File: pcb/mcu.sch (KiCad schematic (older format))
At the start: 13 parts, among them J2 CONN_INTEGRALSTICK_MCU_DEVICE, U1 STM32F777NIH6‎, U10 DSC6083MI2A-032K768, U2 XC7A50T-1FTG256C, U6 S25FL064LABNFI011‎

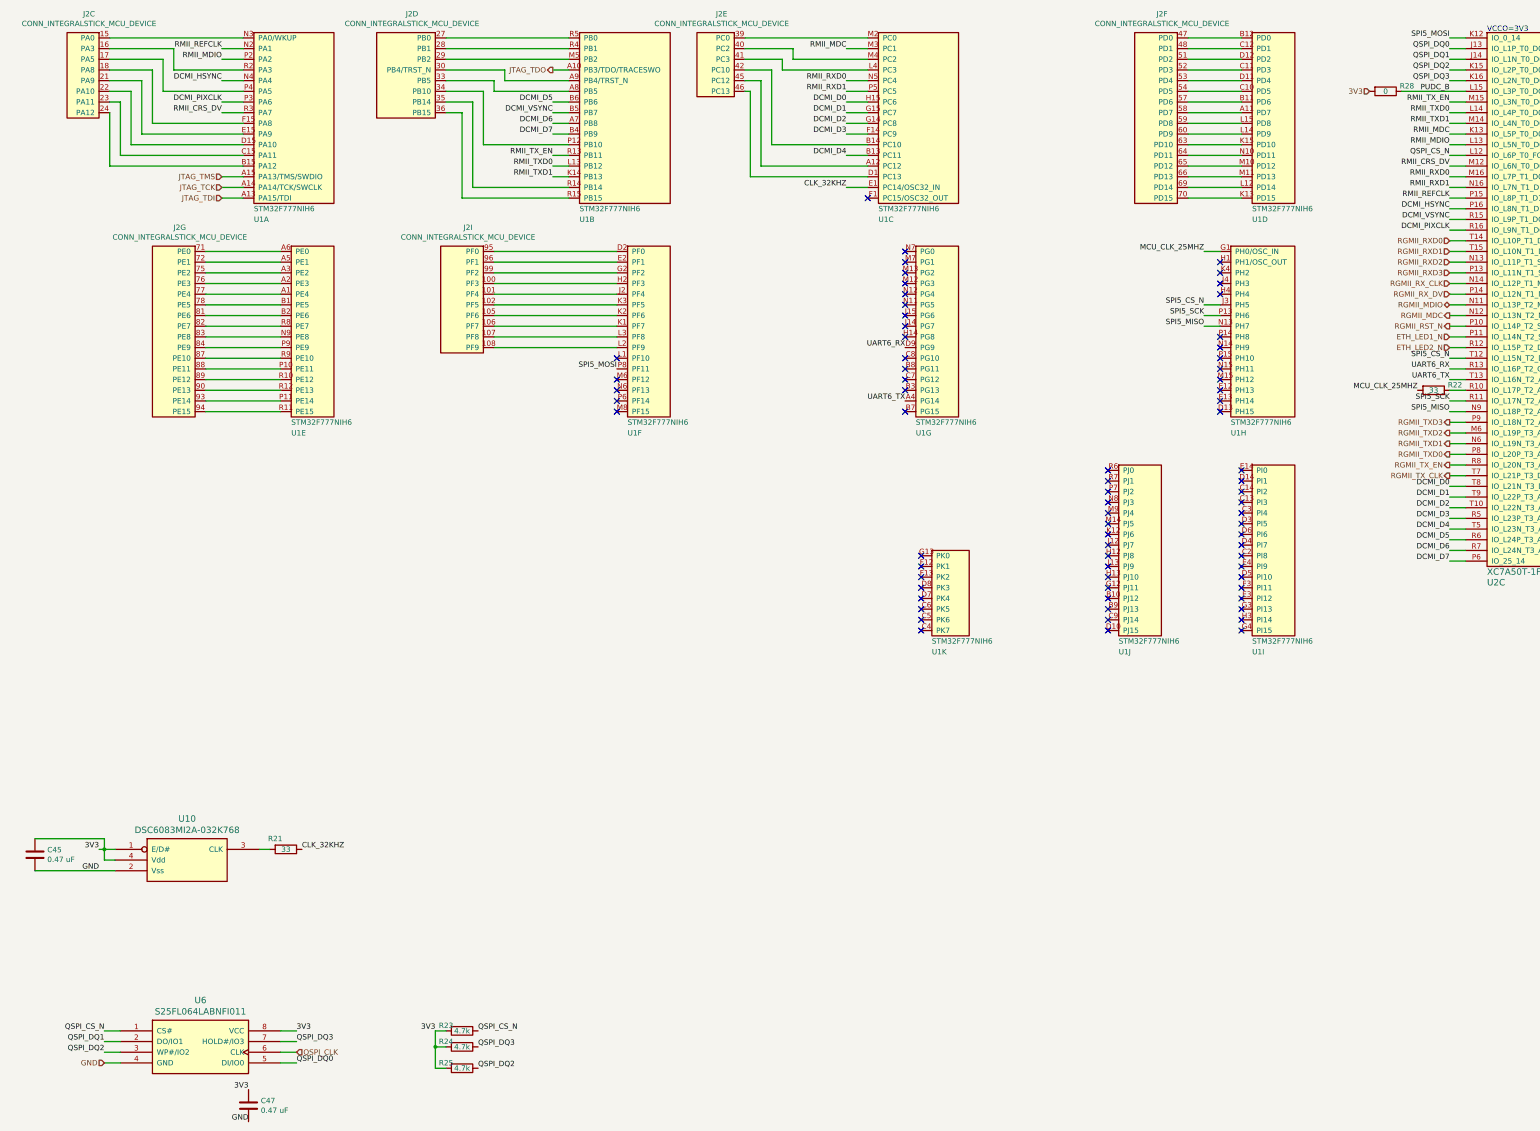
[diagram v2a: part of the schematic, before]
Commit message: Finished schematic signoff review. Fixed oscillator pinout bug, added some test points.
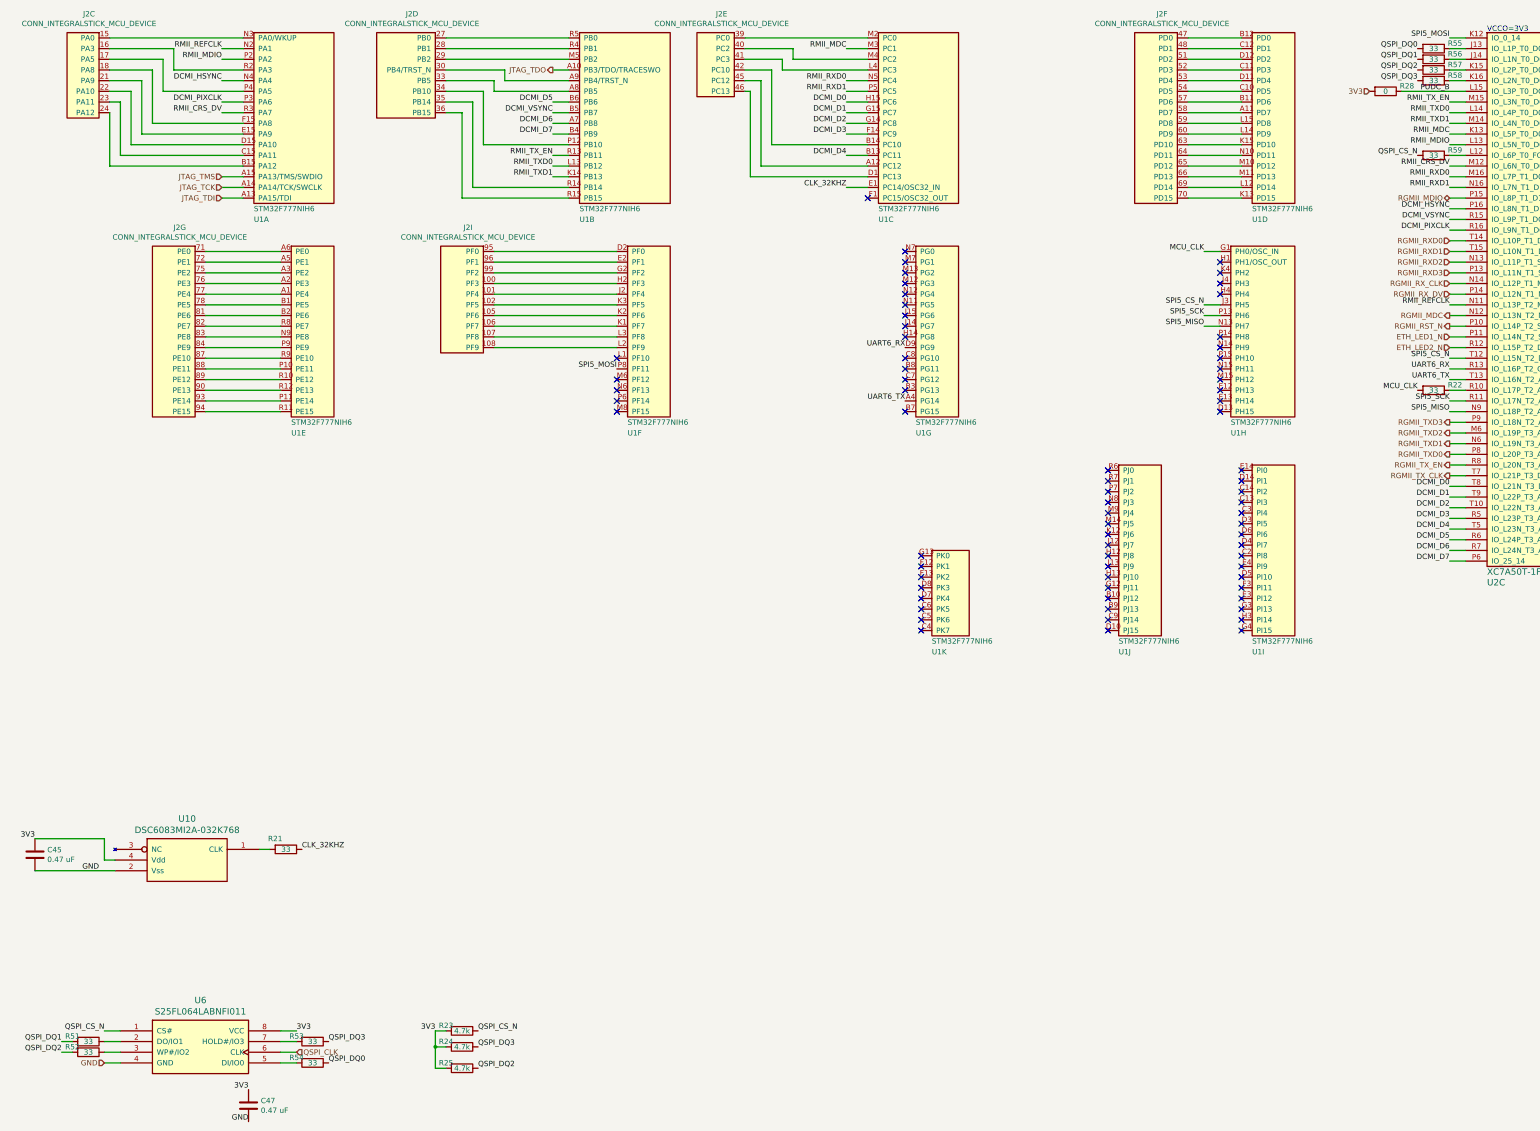
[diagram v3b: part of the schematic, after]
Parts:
- removed U10: DSC6083MI2A-032K768, symbol osc-azonenberg:OSC
- added R51, R52, R53, R54, R55, R56, R57, R58, R59: 33, symbol device:R
- added U10: DSC6083MI2A-032K768, symbol osc-azonenberg:DSC6083
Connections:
- net 3V3: now also U10.4 (Vdd)
- net GND: now also U10.2 (Vss)
- net QSPI_CS_N: now also R59.2; no longer U2.L12 (IO_L6P_T0_FCS_B_14)
- net QSPI_DQ0: now also R54.1, R55.2; no longer U2.J13 (IO_L1P_T0_D00_MOSI_14), U6.5 (DI/IO0)
- net QSPI_DQ1: now also R51.2, R56.2; no longer U2.J14 (IO_L1N_T0_D01_DIN_14), U6.2 (DO/IO1)
- net QSPI_DQ2: now also R52.2, R57.2; no longer U2.K15 (IO_L2P_T0_D02_14), U6.3 (WP#/IO2)
- net QSPI_DQ3: now also R53.1, R58.2; no longer U2.K16 (IO_L2N_T0_D03_14), U6.7 (HOLD#/IO3)
- net RGMII_MDIO: now also U2.P15 (IO_L8P_T1_D11_14); no longer U2.N11 (IO_L13P_T2_MRCC_14)
- net RMII_REFCLK: now also U2.N11 (IO_L13P_T2_MRCC_14); no longer U2.P15 (IO_L8P_T1_D11_14)
- net at R21.2: now also U10.1 (CLK)
- net MCU_CLK_25MHZ renamed MCU_CLK
- new net: R55.1, U2.J13 (IO_L1P_T0_D00_MOSI_14)
- new net: R56.1, U2.J14 (IO_L1N_T0_D01_DIN_14)
- new net: R57.1, U2.K15 (IO_L2P_T0_D02_14)
- new net: R58.1, U2.K16 (IO_L2N_T0_D03_14)
- new net: R59.1, U2.L12 (IO_L6P_T0_FCS_B_14)
- new net: R51.1, U6.2 (DO/IO1)
- new net: R52.1, U6.3 (WP#/IO2)
- new net: R54.2, U6.5 (DI/IO0)
- new net: R53.2, U6.7 (HOLD#/IO3)
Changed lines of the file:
@@
 Sheet 8 8
 Title "INTEGRALSTICK Compute Module"
-Date "2018-11-07"
+Date "2018-11-09"
 Rev "0.1"
 Comp "Andrew D. Zonenberg"
@@
 Text Label 13950 5450 2    50   ~ 0
 DCMI_D4
-Text Label 13950 2350 2    50   ~ 0
+Text Label 13950 3350 2    50   ~ 0
 RMII_REFCLK
 Text Label 13950 1850 2    50   ~ 0
@@
 Wire Wire Line
 	1350 10450 1500 10450
-Text Label 3150 10450 0    50   ~ 0
+Text Label 3450 10450 0    50   ~ 0
 QSPI_DQ0
-Text Label 1350 10250 2    50   ~ 0
+Text Label 950  10250 2    50   ~ 0
 QSPI_DQ1
 Text Label 1350 10150 2    50   ~ 0
@@
 Wire Wire Line
 	3150 10450 3000 10450
-Text Label 1350 10350 2    50   ~ 0
+Text Label 950  10350 2    50   ~ 0
 QSPI_DQ2
-Text Label 3150 10250 0    50   ~ 0
+Text Label 3450 10250 0    50   ~ 0
 QSPI_DQ3
 Wire Wire Line
@@
 Wire Wire Line
 	3000 10250 3150 10250
-Text Label 13950 950  2    50   ~ 0
+Text Label 13650 950  2    50   ~ 0
 QSPI_DQ0
-Text Label 13950 1050 2    50   ~ 0
+Text Label 13650 1050 2    50   ~ 0
 QSPI_DQ1
-Text Label 13950 1150 2    50   ~ 0
+Text Label 13650 1150 2    50   ~ 0
 QSPI_DQ2
-Text Label 13950 1250 2    50   ~ 0
+Text Label 13650 1250 2    50   ~ 0
 QSPI_DQ3
 Wire Wire Line
@@
 Wire Wire Line
 	14100 950  13950 950
-Text Label 13950 1950 2    50   ~ 0
+Text Label 13650 1950 2    50   ~ 0
 QSPI_CS_N
 Wire Wire Line
@@
 	13950 2250 14100 2250
 Wire Wire Line
-	14100 2350 13950 2350
+	14100 3350 13950 3350
 Wire Wire Line
 	14100 2650 13950 2650
@@
 Wire Wire Line
 	14100 3250 13950 3250
-Text HLabel 13950 3350 0    50   BiDi ~ 0
+Text HLabel 13950 2350 0    50   BiDi ~ 0
 RGMII_MDIO
 Text HLabel 13950 3450 0    50   Output ~ 0
@@
 	13950 3450 14100 3450
 Wire Wire Line
-	14100 3350 13950 3350
+	14100 2350 13950 2350
 Text HLabel 13950 3550 0    50   Output ~ 0
 RGMII_RST_N
@@
 GND
 NoConn ~ 11800 2950
-$Comp
-L osc-azonenberg:OSC U10
-U 1 1 5BE5F5BA
-P 2150 8450
-F 0 "U10" H 2125 8737 60  0000 C CNN
-F 1 "DSC6083MI2A-032K768" H 2125 8631 60  0000 C CNN
-F 2 "" H 2150 8450 60  0000 C CNN
-F 3 "" H 2150 8450 60  0000 C CNN
-	1    2150 8450
-	1    0    0    -1
-$EndComp
-Text Label 1300 8450 2    50   ~ 0
+Text Label 700  8350 2    50   ~ 0
 3V3
 Wire Wire Line
-	1300 8450 1350 8450
-Wire Wire Line
-	1350 8450 1350 8550
-Wire Wire Line
 	1350 8550 1450 8550
-Connection ~ 1350 8450
-Wire Wire Line
-	1350 8450 1450 8450
 Text Label 1300 8650 2    50   ~ 0
 GND
@@
 Wire Wire Line
 	700  8350 1350 8350
-Wire Wire Line
-	1350 8350 1350 8450
 Text Label 8300 2250 2    50   ~ 0
 CLK_32KHZ
@@
 $EndComp
 Text Label 13650 4150 2    50   ~ 0
-MCU_CLK_25MHZ
+MCU_CLK
 Text Label 11650 2850 2    50   ~ 0
-MCU_CLK_25MHZ
+MCU_CLK
 Wire Wire Line
 	11650 2850 11800 2850
@@
 Wire Wire Line
 	13950 4350 14100 4350
+$Comp
+L osc-azonenberg:DSC6083 U10
+U 1 1 5D305E88
+P 2150 8450
+F 0 "U10" H 2125 8737 60  0000 C CNN
+F 1 "DSC6083MI2A-032K768" H 2125 8631 60  0000 C CNN
+F 2 "" H 2150 8450 60  0000 C CNN
+F 3 "" H 2150 8450 60  0000 C CNN
+	1    2150 8450
+	1    0    0    -1
+$EndComp
+Wire Wire Line
+	1350 8350 1350 8550
+$Comp
+L device:R R53
+U 1 1 5D3680F9
+P 3300 10250
+F 0 "R53" V 3250 10100 50  0000 C CNN
+F 1 "33" V 3300 10250 50  0000 C CNN
+F 2 "" V 3230 10250 50  0001 C CNN
+F 3 "" H 3300 10250 50  0001 C CNN
+	1    3300 10250
+	0    1    1    0
+$EndComp
+$Comp
+L device:R R54
+U 1 1 5D3687A9
+P 3300 10450
+F 0 "R54" V 3250 10300 50  0000 C CNN
+F 1 "33" V 3300 10450 50  0000 C CNN
+F 2 "" V 3230 10450 50  0001 C CNN
+F 3 "" H 3300 10450 50  0001 C CNN
+	1    3300 10450
+	0    1    1    0
+$EndComp
+$Comp
+L device:R R52
+U 1 1 5D368B11
+P 1200 10350
+F 0 "R52" V 1150 10200 50  0000 C CNN
+F 1 "33" V 1200 10350 50  0000 C CNN
+F 2 "" V 1130 10350 50  0001 C CNN
+F 3 "" H 1200 10350 50  0001 C CNN
+	1    1200 10350
+	0    1    1    0
+$EndComp
+$Comp
+L device:R R51
+U 1 1 5D379C82
+P 1200 10250
+F 0 "R51" V 1150 10100 50  0000 C CNN
+F 1 "33" V 1200 10250 50  0000 C CNN
+F 2 "" V 1130 10250 50  0001 C CNN
+F 3 "" H 1200 10250 50  0001 C CNN
+	1    1200 10250
+	0    1    1    0
+$EndComp
+Wire Wire Line
+	950  10250 1050 10250
+Wire Wire Line
+	1050 10350 950  10350
+$Comp
+L device:R R55
+U 1 1 5D3D3279
+P 13800 950
+F 0 "R55" V 13750 1150 50  0000 C CNN
+F 1 "33" V 13800 950 50  0000 C CNN
+F 2 "" V 13730 950 50  0001 C CNN
+F 3 "" H 13800 950 50  0001 C CNN
+	1    13800 950
+	0    1    1    0
+$EndComp
+$Comp
+L device:R R56
+U 1 1 5D3D36A5
+P 13800 1050
+F 0 "R56" V 13750 1250 50  0000 C CNN
+F 1 "33" V 13800 1050 50  0000 C CNN
+F 2 "" V 13730 1050 50  0001 C CNN
+F 3 "" H 13800 1050 50  0001 C CNN
+	1    13800 1050
+	0    1    1    0
+$EndComp
+$Comp
+L device:R R57
+U 1 1 5D3D390E
+P 13800 1150
+F 0 "R57" V 13750 1350 50  0000 C CNN
+F 1 "33" V 13800 1150 50  0000 C CNN
+F 2 "" V 13730 1150 50  0001 C CNN
+F 3 "" H 13800 1150 50  0001 C CNN
+	1    13800 1150
+	0    1    1    0
+$EndComp
+$Comp
+L device:R R58
+U 1 1 5D3D3C3B
+P 13800 1250
+F 0 "R58" V 13750 1450 50  0000 C CNN
+F 1 "33" V 13800 1250 50  0000 C CNN
+F 2 "" V 13730 1250 50  0001 C CNN
+F 3 "" H 13800 1250 50  0001 C CNN
+	1    13800 1250
+	0    1    1    0
+$EndComp
+$Comp
+L device:R R59
+U 1 1 5D3E7347
+P 13800 1950
+F 0 "R59" V 13750 2150 50  0000 C CNN
+F 1 "33" V 13800 1950 50  0000 C CNN
+F 2 "" V 13730 1950 50  0001 C CNN
+F 3 "" H 13800 1950 50  0001 C CNN
+	1    13800 1950
+	0    1    1    0
+$EndComp
 $EndSCHEMATC

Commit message: Assigned lots of footprints. Still have a few to go.
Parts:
- C45, C47: footprint (none) -> azonenberg_pcb:EIA_0402_CAP_NOSILK
- J2: footprint (none) -> azonenberg_pcb:CONN_SAMTEC_QTH-060-01-L-D-A
- R21, R22, R23, R24, R25, R28, R51, R52, R53, R54, R55, R56, R57, R58, R59: footprint (none) -> azonenberg_pcb:EIA_0402_RES_NOSILK
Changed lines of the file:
@@
 F 0 "J2" H 1394 2575 50  0000 C CNN
 F 1 "CONN_INTEGRALSTICK_MCU_DEVICE" H 1394 2484 50  0000 C CNN
-F 2 "" H 1300 1600 50  0001 C CNN
+F 2 "azonenberg_pcb:CONN_SAMTEC_QTH-060-01-L-D-A" H 1300 1600 50  0001 C CNN
 F 3 "" H 1300 1600 50  0001 C CNN
 	3    1300 1600
@@
 F 0 "J2" H 4669 2575 50  0000 C CNN
 F 1 "CONN_INTEGRALSTICK_MCU_DEVICE" H 4669 2484 50  0000 C CNN
-F 2 "" H 4450 1600 50  0001 C CNN
+F 2 "azonenberg_pcb:CONN_SAMTEC_QTH-060-01-L-D-A" H 4450 1600 50  0001 C CNN
 F 3 "" H 4450 1600 50  0001 C CNN
 	4    4450 1600
@@
 F 0 "J2" H 7369 2175 50  0000 C CNN
 F 1 "CONN_INTEGRALSTICK_MCU_DEVICE" H 7369 2084 50  0000 C CNN
-F 2 "" H 7250 1400 50  0001 C CNN
+F 2 "azonenberg_pcb:CONN_SAMTEC_QTH-060-01-L-D-A" H 7250 1400 50  0001 C CNN
 F 3 "" H 7250 1400 50  0001 C CNN
 	5    7250 1400
@@
 F 0 "J2" H 11544 4175 50  0000 C CNN
 F 1 "CONN_INTEGRALSTICK_MCU_DEVICE" H 11544 4084 50  0000 C CNN
-F 2 "" H 11400 2400 50  0001 C CNN
+F 2 "azonenberg_pcb:CONN_SAMTEC_QTH-060-01-L-D-A" H 11400 2400 50  0001 C CNN
 F 3 "" H 11400 2400 50  0001 C CNN
 	6    11400 2400
@@
 F 0 "J2" H 2344 6175 50  0000 C CNN
 F 1 "CONN_INTEGRALSTICK_MCU_DEVICE" H 2344 6084 50  0000 C CNN
-F 2 "" H 2200 4400 50  0001 C CNN
+F 2 "azonenberg_pcb:CONN_SAMTEC_QTH-060-01-L-D-A" H 2200 4400 50  0001 C CNN
 F 3 "" H 2200 4400 50  0001 C CNN
 	7    2200 4400
@@
 F 0 "J2" H 5044 4975 50  0000 C CNN
 F 1 "CONN_INTEGRALSTICK_MCU_DEVICE" H 5044 4884 50  0000 C CNN
-F 2 "" H 4900 3800 50  0001 C CNN
+F 2 "azonenberg_pcb:CONN_SAMTEC_QTH-060-01-L-D-A" H 4900 3800 50  0001 C CNN
 F 3 "" H 4900 3800 50  0001 C CNN
 	9    4900 3800
@@
 F 0 "R23" V 4650 10000 50  0000 C CNN
 F 1 "4.7k" V 4700 10150 50  0000 C CNN
-F 2 "" V 4630 10150 50  0001 C CNN
+F 2 "azonenberg_pcb:EIA_0402_RES_NOSILK" V 4630 10150 50  0001 C CNN
 F 3 "" H 4700 10150 50  0001 C CNN
 	1    4700 10150
@@
 F 0 "R24" V 4650 10150 50  0000 C CNN
 F 1 "4.7k" V 4700 10300 50  0000 C CNN
-F 2 "" V 4630 10300 50  0001 C CNN
+F 2 "azonenberg_pcb:EIA_0402_RES_NOSILK" V 4630 10300 50  0001 C CNN
 F 3 "" H 4700 10300 50  0001 C CNN
 	1    4700 10300
@@
 F 0 "R25" V 4650 10350 50  0000 C CNN
 F 1 "4.7k" V 4700 10500 50  0000 C CNN
-F 2 "" V 4630 10500 50  0001 C CNN
+F 2 "azonenberg_pcb:EIA_0402_RES_NOSILK" V 4630 10500 50  0001 C CNN
 F 3 "" H 4700 10500 50  0001 C CNN
 	1    4700 10500
@@
 F 0 "C47" H 2815 10896 50  0000 L CNN
 F 1 "0.47 uF" H 2815 10805 50  0000 L CNN
-F 2 "" H 2738 10700 50  0001 C CNN
+F 2 "azonenberg_pcb:EIA_0402_CAP_NOSILK" H 2738 10700 50  0001 C CNN
 F 3 "" H 2700 10850 50  0001 C CNN
 	1    2700 10850
@@
 F 0 "R21" V 2950 8350 50  0000 C CNN
 F 1 "33" V 3050 8450 50  0000 C CNN
-F 2 "" V 2980 8450 50  0001 C CNN
+F 2 "azonenberg_pcb:EIA_0402_RES_NOSILK" V 2980 8450 50  0001 C CNN
 F 3 "" H 3050 8450 50  0001 C CNN
 	1    3050 8450
@@
 F 0 "C45" H 815 8546 50  0000 L CNN
 F 1 "0.47 uF" H 815 8455 50  0000 L CNN
-F 2 "" H 738 8350 50  0001 C CNN
+F 2 "azonenberg_pcb:EIA_0402_CAP_NOSILK" H 738 8350 50  0001 C CNN
 F 3 "" H 700 8500 50  0001 C CNN
 	1    700  8500
@@
 F 0 "R22" V 13750 4350 50  0000 C CNN
 F 1 "33" V 13800 4150 50  0000 C CNN
-F 2 "" V 13730 4150 50  0001 C CNN
+F 2 "azonenberg_pcb:EIA_0402_RES_NOSILK" V 13730 4150 50  0001 C CNN
 F 3 "" H 13800 4150 50  0001 C CNN
 	1    13800 4150
@@
 F 0 "R28" V 13300 1550 50  0000 C CNN
 F 1 "0" V 13350 1350 50  0000 C CNN
-F 2 "" V 13280 1350 50  0001 C CNN
+F 2 "azonenberg_pcb:EIA_0402_RES_NOSILK" V 13280 1350 50  0001 C CNN
 F 3 "" H 13350 1350 50  0001 C CNN
 	1    13350 1350
@@
 F 0 "U10" H 2125 8737 60  0000 C CNN
 F 1 "DSC6083MI2A-032K768" H 2125 8631 60  0000 C CNN
-F 2 "" H 2150 8450 60  0000 C CNN
+F 2 "" H 2150 8450 60  0001 C CNN
 F 3 "" H 2150 8450 60  0000 C CNN
 	1    2150 8450
@@
 F 0 "R53" V 3250 10100 50  0000 C CNN
 F 1 "33" V 3300 10250 50  0000 C CNN
-F 2 "" V 3230 10250 50  0001 C CNN
+F 2 "azonenberg_pcb:EIA_0402_RES_NOSILK" V 3230 10250 50  0001 C CNN
 F 3 "" H 3300 10250 50  0001 C CNN
 	1    3300 10250
@@
 F 0 "R54" V 3250 10300 50  0000 C CNN
 F 1 "33" V 3300 10450 50  0000 C CNN
-F 2 "" V 3230 10450 50  0001 C CNN
+F 2 "azonenberg_pcb:EIA_0402_RES_NOSILK" V 3230 10450 50  0001 C CNN
 F 3 "" H 3300 10450 50  0001 C CNN
 	1    3300 10450
@@
 F 0 "R52" V 1150 10200 50  0000 C CNN
 F 1 "33" V 1200 10350 50  0000 C CNN
-F 2 "" V 1130 10350 50  0001 C CNN
+F 2 "azonenberg_pcb:EIA_0402_RES_NOSILK" V 1130 10350 50  0001 C CNN
 F 3 "" H 1200 10350 50  0001 C CNN
 	1    1200 10350
@@
 F 0 "R51" V 1150 10100 50  0000 C CNN
 F 1 "33" V 1200 10250 50  0000 C CNN
-F 2 "" V 1130 10250 50  0001 C CNN
+F 2 "azonenberg_pcb:EIA_0402_RES_NOSILK" V 1130 10250 50  0001 C CNN
 F 3 "" H 1200 10250 50  0001 C CNN
 	1    1200 10250
@@
 F 0 "R55" V 13750 1150 50  0000 C CNN
 F 1 "33" V 13800 950 50  0000 C CNN
-F 2 "" V 13730 950 50  0001 C CNN
+F 2 "azonenberg_pcb:EIA_0402_RES_NOSILK" V 13730 950 50  0001 C CNN
 F 3 "" H 13800 950 50  0001 C CNN
 	1    13800 950
@@
 F 0 "R56" V 13750 1250 50  0000 C CNN
 F 1 "33" V 13800 1050 50  0000 C CNN
-F 2 "" V 13730 1050 50  0001 C CNN
+F 2 "azonenberg_pcb:EIA_0402_RES_NOSILK" V 13730 1050 50  0001 C CNN
 F 3 "" H 13800 1050 50  0001 C CNN
 	1    13800 1050
@@
 F 0 "R57" V 13750 1350 50  0000 C CNN
 F 1 "33" V 13800 1150 50  0000 C CNN
-F 2 "" V 13730 1150 50  0001 C CNN
+F 2 "azonenberg_pcb:EIA_0402_RES_NOSILK" V 13730 1150 50  0001 C CNN
 F 3 "" H 13800 1150 50  0001 C CNN
 	1    13800 1150
@@
 F 0 "R58" V 13750 1450 50  0000 C CNN
 F 1 "33" V 13800 1250 50  0000 C CNN
-F 2 "" V 13730 1250 50  0001 C CNN
+F 2 "azonenberg_pcb:EIA_0402_RES_NOSILK" V 13730 1250 50  0001 C CNN
 F 3 "" H 13800 1250 50  0001 C CNN
 	1    13800 1250
@@
 F 0 "R59" V 13750 2150 50  0000 C CNN
 F 1 "33" V 13800 1950 50  0000 C CNN
-F 2 "" V 13730 1950 50  0001 C CNN
+F 2 "azonenberg_pcb:EIA_0402_RES_NOSILK" V 13730 1950 50  0001 C CNN
 F 3 "" H 13800 1950 50  0001 C CNN
 	1    13800 1950

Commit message: Finished initial footprint assignments
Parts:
- U10: footprint (none) -> azonenberg_pcb:OSCILLATOR_2.0x1.6
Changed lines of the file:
@@
 F 0 "U10" H 2125 8737 60  0000 C CNN
 F 1 "DSC6083MI2A-032K768" H 2125 8631 60  0000 C CNN
-F 2 "" H 2150 8450 60  0001 C CNN
+F 2 "azonenberg_pcb:OSCILLATOR_2.0x1.6" H 2150 8450 60  0001 C CNN
 F 3 "" H 2150 8450 60  0000 C CNN
 	1    2150 8450

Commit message: Initial work on FPGA fanout
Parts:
- R28: footprint azonenberg_pcb:EIA_0402_RES_NOSILK -> azonenberg_pcb:EIA_0402_CAP_NOSILK
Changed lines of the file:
@@
 F 0 "R28" V 13300 1550 50  0000 C CNN
 F 1 "0" V 13350 1350 50  0000 C CNN
-F 2 "azonenberg_pcb:EIA_0402_RES_NOSILK" V 13280 1350 50  0001 C CNN
+F 2 "azonenberg_pcb:EIA_0402_CAP_NOSILK" V 13280 1350 50  0001 C CNN
 F 3 "" H 13350 1350 50  0001 C CNN
 	1    13350 1350

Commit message: Finished first iteration layout of RAM. Lots of pin swaps.
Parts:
- U2: footprint azonenberg_pcb:BGA_256_17x17_FULLARRAY_1MM -> azonenberg_pcb:BGA_256_17x17_FULLARRAY_1MM_0.4MM_FTG256
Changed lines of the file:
@@
 Sheet 8 8
 Title "INTEGRALSTICK Compute Module"
-Date "2018-11-09"
+Date "2018-11-11"
 Rev "0.1"
 Comp "Andrew D. Zonenberg"
@@
 F 0 "U2" H 14300 5550 60  0000 L CNN
 F 1 "XC7A50T-1FTG256C" H 14300 5650 60  0000 L CNN
-F 2 "azonenberg_pcb:BGA_256_17x17_FULLARRAY_1MM" H 14300 5750 60  0001 C CNN
+F 2 "azonenberg_pcb:BGA_256_17x17_FULLARRAY_1MM_0.4MM_FTG256" H 14300 5750 60  0001 C CNN
 F 3 "" H 14300 5750 60  0000 C CNN
 	3    14300 5750
